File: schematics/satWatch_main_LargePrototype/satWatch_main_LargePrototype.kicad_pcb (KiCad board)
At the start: 2 copper layers, 9.2 x 7 mm, 88 parts, among them J1 PogoPins_02x17_Data, J2 UJ20-C-H-G-MSMT-2B-P16-TR, J5 Pogo_02x03_Power, Q1 FS8205, Q2 BSS138, Q3 DMP1045U, Q4 BSS138, SW1 B3U-1000P, SW2 B3U-1000P, SW3 B3U-1000P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

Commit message: v0.3
Finalized initial draft of large mainboard PCB, ready for first production and testing
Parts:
- added C21: 1uF, Capacitor_SMD:C_0603_1608Metric_Pad1.08x0.95mm_HandSolder, F.Cu at (186.6, 71.7)
- added C22: 1uF, Capacitor_SMD:C_0603_1608Metric_Pad1.08x0.95mm_HandSolder, F.Cu at (188.2, 80.3)
- added C23: 1uF, Capacitor_SMD:C_0603_1608Metric_Pad1.08x0.95mm_HandSolder, F.Cu at (181.2, 77.0)
- added C24: 22pF, Capacitor_SMD:C_0603_1608Metric_Pad1.08x0.95mm_HandSolder, F.Cu at (207.0, 103.7)
- added C25: 22pF, Capacitor_SMD:C_0603_1608Metric_Pad1.08x0.95mm_HandSolder, F.Cu at (209.5, 103.8)
- added C26: 0.1uF, Capacitor_SMD:C_0603_1608Metric_Pad1.08x0.95mm_HandSolder, F.Cu at (207.5, 90.6)
- added C27: 0.1uF, Capacitor_SMD:C_0603_1608Metric_Pad1.08x0.95mm_HandSolder, F.Cu at (212.1, 99.2)
- added C5: 1uF, Capacitor_SMD:C_0603_1608Metric_Pad1.08x0.95mm_HandSolder, F.Cu at (200.7, 74.1)
- added LED1: SFH 7016, footprint:SFH7016, B.Cu at (203.8, 77.5)
- added R26: 10K, Resistor_SMD:R_0603_1608Metric_Pad0.98x0.95mm_HandSolder, F.Cu at (213.0, 90.5)
- added R27: 10, Resistor_SMD:R_0603_1608Metric_Pad0.98x0.95mm_HandSolder, F.Cu at (181.3, 79.0)
- added R28: 100K, Resistor_SMD:R_0603_1608Metric_Pad0.98x0.95mm_HandSolder, F.Cu at (196.0, 82.2)
- added R29: 0, Resistor_SMD:R_0603_1608Metric_Pad0.98x0.95mm_HandSolder, F.Cu at (204.3, 77.6)
- added R30: 0, Resistor_SMD:R_0603_1608Metric_Pad0.98x0.95mm_HandSolder, F.Cu at (204.3, 75.6)
- added R31: 0, Resistor_SMD:R_0603_1608Metric_Pad0.98x0.95mm_HandSolder, F.Cu at (204.3, 79.5)
- added R32: 0, Resistor_SMD:R_0603_1608Metric_Pad0.98x0.95mm_HandSolder, F.Cu at (212.9, 94.5)
- added R33: 0, Resistor_SMD:R_0603_1608Metric_Pad0.98x0.95mm_HandSolder, F.Cu at (213.0, 92.3)
- added R6: 10K, Resistor_SMD:R_0603_1608Metric_Pad0.98x0.95mm_HandSolder, F.Cu at (213.0, 96.2)
- added TP23: PPG_MISO, TestPoint:TestPoint_Pad_D2.5mm, F.Cu at (190.9, 69.5)
- added TP24: PPG_MOSI, TestPoint:TestPoint_Pad_D2.5mm, F.Cu at (195.1, 69.5)
- added TP25: PPG_SCK, TestPoint:TestPoint_Pad_D2.5mm, F.Cu at (195.3, 74.4)
- added TP26: PPG_CSB, TestPoint:TestPoint_Pad_D2.5mm, F.Cu at (190.9, 74.5)
- added TP27: PPG_INT, TestPoint:TestPoint_Pad_D2.5mm, F.Cu at (192.5, 79.3)
- added U10: VEMD8080, footprint:VEMD8080, B.Cu at (202.7, 74.4)
- added U11: VEMD8080, footprint:VEMD8080, B.Cu at (202.6, 81.2)
- added U12: BNO085, footprint:IC_BNO085, F.Cu at (207.0, 95.2)
- added U3: MAX32664GTGC, footprint:MAX32664GTGB+T, F.Cu at (186.7, 76.2)
- added Y1: 32.768kHz, footprint:ABS07-32.768KHZ-T, F.Cu at (185.0, 80.5)
- added Y2: 32.768Hz, footprint:ABS07-32.768KHZ-T, F.Cu at (208.2, 100.5)
- U2: value MAX30101EFD_T -> MAX86141; footprint footprint:PSON80P560X330X165-14N -> footprint:MAX86141ENP
- moved C10 13.1 mm to (200.9, 81.8), turned to -90 degrees
- moved U2 11.9 mm to (200.0, 77.3), turned to 90 degrees
- moved C9 9.52 mm to (198.9, 81.8), turned to -90 degrees
- moved C4 8.25 mm to (156.7, 75.3)
- moved R21 2.05 mm to (172.5, 78.5), turned to -90 degrees
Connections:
- net /VCC_3V3 renamed VCC_3V3
- C10 pad 1: /VCC_1V8 -> 5V
- C12 pad 1: /VCC_1V8 -> 1V8
- C17 pad 1: /IC_5V -> 5V
- C6 pad 1: /VUSB_5V -> USB_5V
- C9 pad 1: /IC_5V -> 5V
- J1 pad 17: /GPIO33 -> /GPIO47
- J1 pad 18: /LV_SDA -> /GPIO33
- J1 pad 19: /LV_SCL -> /GPIO34
- J1 pad 20: /U0RXD -> /GPIO48
- J1 pad 21: /U0TXD -> /GPIO35
- J1 pad 22: /GPIO48 -> /GPIO36
- J1 pad 23: /GPIO47 -> /GPIO37
- J1 pad 24: /GPIO46 -> /GPIO38
- J1 pad 25: /GPIO45 -> /GPIO39
- J1 pad 26: /GPIO42 -> /GPIO40
- J1 pad 28: /GPIO40 -> /GPIO42
- J1 pad 29: /GPIO39 -> /U0TXD
- J1 pad 30: /GPIO38 -> /U0RXD
- J1 pad 31: /GPIO37 -> /GPIO45
- J1 pad 32: /GPIO36 -> /GPIO46
- J1 pad 33: /GPIO35 -> /LV_SDA
- J1 pad 34: /GPIO34 -> /LV_SCL
- J2 pad A4/B9: /VUSB_5V -> USB_5V
- J2 pad B4/A9: /VUSB_5V -> USB_5V
- R11 pad 2: /VUSB_5V -> USB_5V
- R3 pad 2: /IC_5V -> 5V
- TP5 pad 1: /VUSB_5V -> USB_5V
- TP8 pad 1: /VCC_1V8 -> 1V8
- TP9 pad 1: /IC_5V -> 5V
- U4 pad 6: /VUSB_5V -> USB_5V
- U4 pad 7: /VUSB_5V -> USB_5V
- U4 pad 8: /VUSB_5V -> USB_5V
- U6 pad 5: /VCC_1V8 -> 1V8
- U7 pad 7: /IC_5V -> 5V
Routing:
- net GND: track 316.3 -> 120.6 mm, vias 0 -> 55
- net /VCC_1V8: track 15.2 -> 149.9 mm, vias 0 -> 6
- net 5V: track 0.00 -> 70.0 mm, vias 0 -> 4
- net /GPIO11: track 18.0 -> 76.9 mm, vias 0 -> 2
- net /GPIO10: track 16.4 -> 75.1 mm, vias 0 -> 2
- net 1V8: track 0.00 -> 46.4 mm, vias 0 -> 4
- net /U0RXD: track 72.2 -> 27.0 mm, vias 2 -> 0
- net /U0TXD: track 66.1 -> 28.7 mm, vias 2 -> 0
- net /GPIO42: track 58.5 -> 24.3 mm
- net /GPIO46: track 65.4 -> 31.5 mm
- net /LV_SDA: track 18.4 -> 52.1 mm, vias 0 -> 4
- net /GPIO40: track 52.2 -> 21.6 mm
- net /ESP_3V3: track 59.2 -> 30.9 mm, vias 4 -> 2
- net /VUSB_5V: track 52.5 -> 25.0 mm, vias 4 -> 2
- net USB_5V: track 0.00 -> 27.5 mm, vias 0 -> 2
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- added copper zone on B.Cu, net GND
- added copper zone on F.Cu, net GND
- added copper zone on F.Cu, net VCC_3V3
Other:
- board size 9.2 x 7 mm -> 138.8 x 55.6 mm

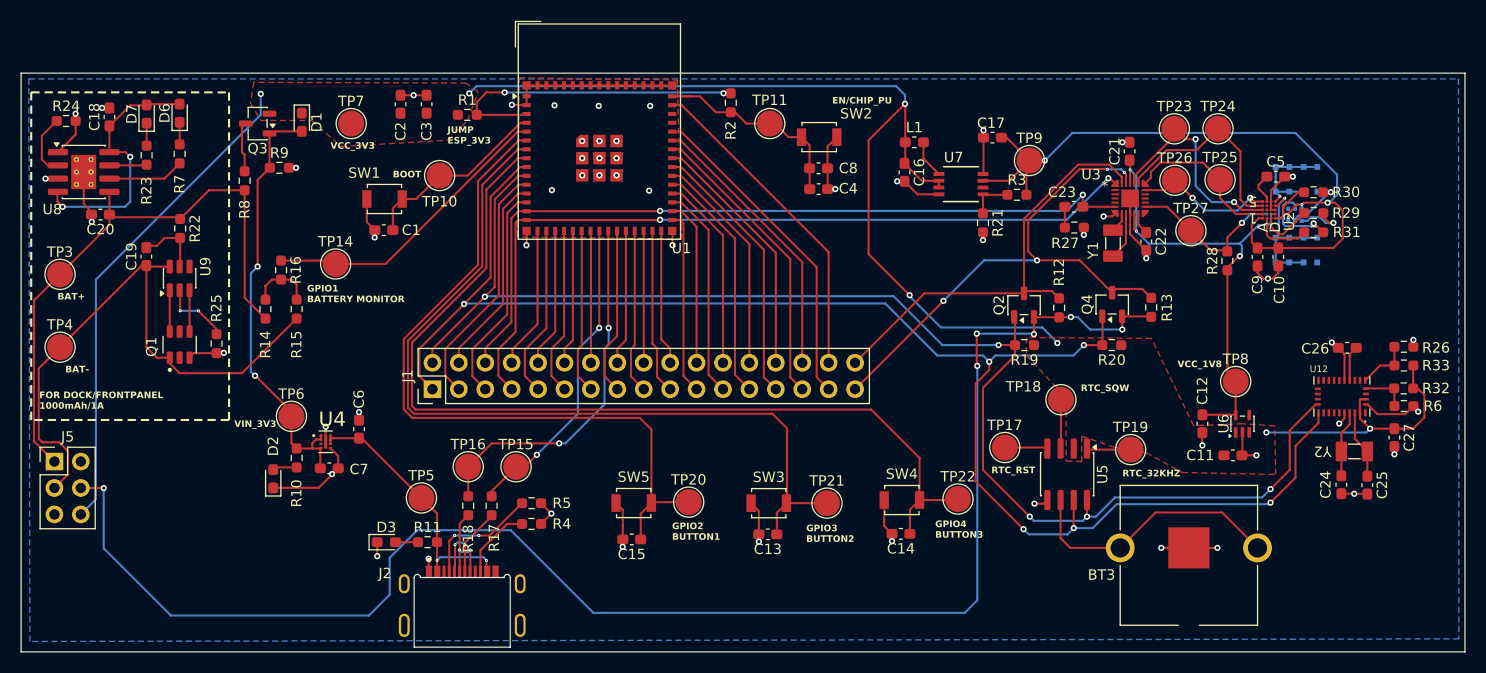
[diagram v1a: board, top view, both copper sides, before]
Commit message: v0.4
Finalized large prototyping PCB for manufacturing
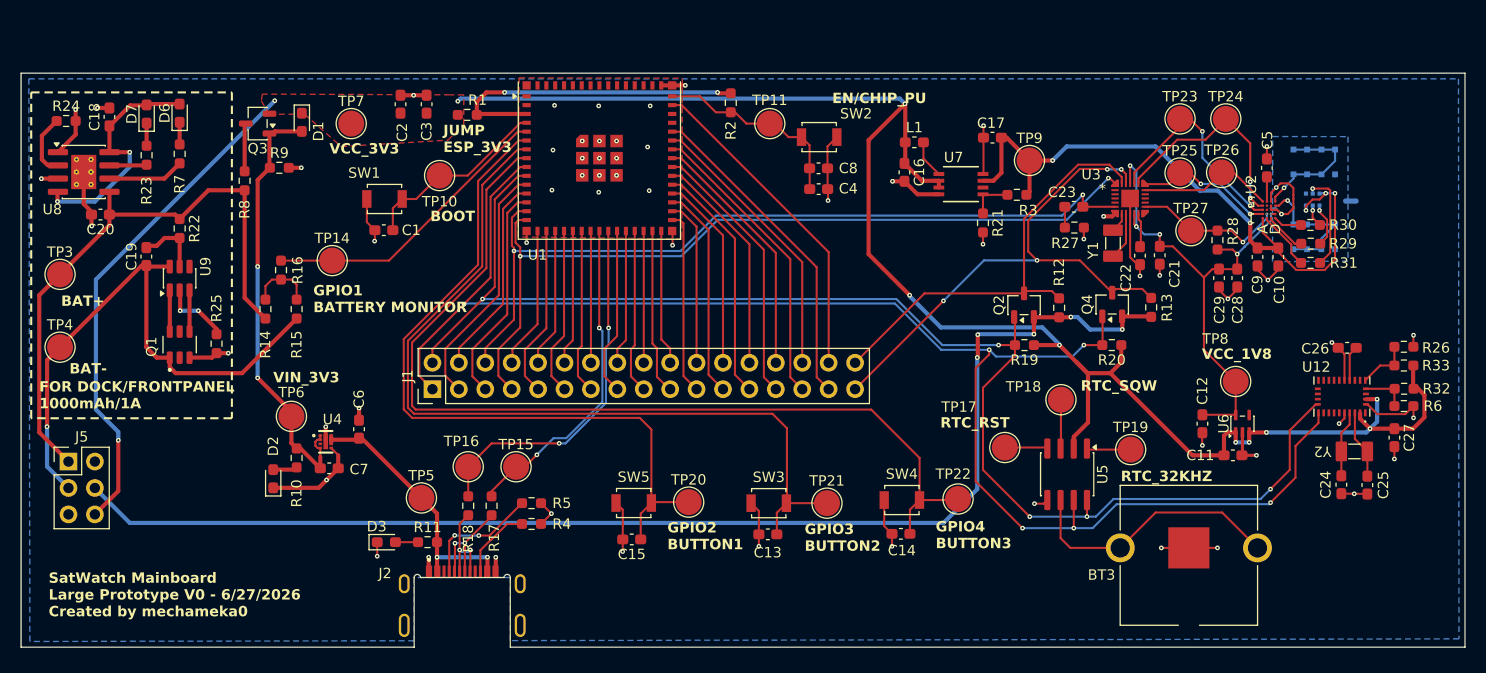
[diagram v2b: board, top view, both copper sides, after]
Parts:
- added C28: 22uF, Capacitor_SMD:C_0603_1608Metric_Pad1.08x0.95mm_HandSolder, F.Cu at (196.9, 83.8)
- added C29: 0.1uF, Capacitor_SMD:C_0603_1608Metric_Pad1.08x0.95mm_HandSolder, F.Cu at (195.2, 83.8)
- added NT1: NetTie_2, footprint:NetTie-2_SMD_Pad0.2mm, F.Cu at (202.3, 76.0)
- added NT1: NetTie_2, NetTie:NetTie-2_SMD_Pad0.5mm, B.Cu at (207.9, 76.5)
- C5: value 1uF -> 10uF
- U1: footprint RF_Module:ESP32-S2-MINI-1 -> footprint:ESP32-S2-MINI-1
- moved C21 10.4 mm to (189.5, 81.7), turned to -90 degrees
- moved TP26 4.56 mm to (195.4, 73.7)
- moved TP25 3.90 mm to (191.4, 73.8)
- moved R30 3.16 mm to (204.0, 78.8)
- moved R29 2.97 mm to (204.0, 80.5)
- moved R31 2.97 mm to (204.0, 82.4)
- moved U10 2.39 mm to (204.4, 72.7)
- moved LED1 2.25 mm to (205.6, 76.1)
- moved R28 2.21 mm to (195.1, 80.2)
- moved U11 2.13 mm to (204.3, 79.9)
- moved C22 1.49 mm to (187.6, 81.7)
- moved J5 1.35 mm to (84.6, 101.5)
- moved TP24 1.21 mm to (195.8, 68.5)
- moved C5 1.20 mm to (199.8, 73.3), turned to 90 degrees
- moved TP23 1.10 mm to (191.4, 68.5)
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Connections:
- U10 pad 5: GND -> /PD_GND
- U11 pad 5: GND -> /PD_GND
- U2 pad C5: GND -> /PD_GND
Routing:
- net VCC_3V3: track 164.4 -> 211.2 mm, vias 7 -> 11
- net /VCC_1V8: track 149.9 -> 122.4 mm, vias 6 -> 5
- net GND: track 120.6 -> 132.7 mm, vias 55 -> 61
- net 5V: track 70.0 -> 63.7 mm, vias 4 -> 5
- net /PD_GND: track 0.00 -> 4.24 mm, vias 0 -> 1
- net Net-(LED1-G): track 5.42 -> 2.16 mm
- net /GPIO10: track 75.1 -> 78.0 mm
- net /PD1_IN: track 10.4 -> 13.0 mm
- net /GPIO11: track 76.9 -> 79.4 mm
- net 1V8: track 46.4 -> 48.7 mm, vias 4 -> 5
- net /VUSB_5V: track 25.0 -> 22.8 mm
- net /PPG_SCK: track 15.5 -> 13.5 mm, vias 0 -> 2
- net /BAT-: track 56.6 -> 54.7 mm, vias 0 -> 1
- net /EN/CHIP_PU: track 21.3 -> 19.4 mm
- net USB_5V: track 27.5 -> 25.7 mm
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- added copper zone on B.Cu, net /PD_GND
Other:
- board size 138.8 x 55.6 mm -> 138.8 x 55.2 mm
- board text added: "SatWatch Mainboard Large Prototype V0 - 6/27/2026 Created by mechameka0"
